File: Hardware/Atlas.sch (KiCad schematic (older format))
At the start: 31 parts, among them U1 MS5611, U2 HTU21D, U3 uSD Card, U4 RFD900, U5 MPU9150, U6 XBEE, U7 VENUS838LPX-L

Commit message: Add 5v regulator and remove before flight switch
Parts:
- added C?: C, ~, symbol C
- added C? (x3): 10uF, CAPC2012-N, symbol C
- added J?: DC, ~, symbol CONN-DC-JACK
- added L?: 4.7uH, INDC-SRN4018, symbol L
- added R?: 52.3k, RESC1608-N, symbol R
- added R?: R, ~, symbol R
- added R?: 10k, RESC1608-N, symbol R
- added U?: AOZ1031, ~, symbol AOZ1031
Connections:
- wire segments 158 -> 193
- no-connect marks 31 -> 40
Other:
- moved on the sheet: B1, H1B, H1C

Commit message: Connect serial peripherals
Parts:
- gave numbers to parts that had none: 10
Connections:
- wire segments 193 -> 267

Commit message: Remove split GPS ground
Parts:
- removed R5: 0, RESC1608-N, symbol R
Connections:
- net labels removed: AGND
- wire segments 267 -> 194

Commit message: Majority of layout and routing
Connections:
- net +5V: no longer H1.D18 (5V)
- net LX: now reaches L2.1, U8.7 (L), U8.8 (L)
- no-connect marks 40 -> 43
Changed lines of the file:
@@
 Sheet 1 1
 Title "Atlas (Nucleo Shield)"
-Date "24 may 2014"
+Date "25 may 2014"
 Rev "1"
 Comp "Aerodyne Labs"
@@
 Connection ~ 2700 9400
 Wire Wire Line
-	2800 8300 2800 9200
-Wire Wire Line
 	2800 8600 2500 8600
-Wire Wire Line
-	2800 9200 2500 9200
-Connection ~ 2800 8600
 Wire Wire Line
 	2600 8300 2600 9100
@@
 	10300 1800 10300 2000
 Connection ~ 10100 2200
+Text Label 14000 1700 2    60   ~ 0
+LX
+Wire Wire Line
+	2800 8300 2800 8600
+NoConn ~ 2500 9200
+NoConn ~ 1500 9000
+NoConn ~ 1500 9100
 $EndSCHEMATC

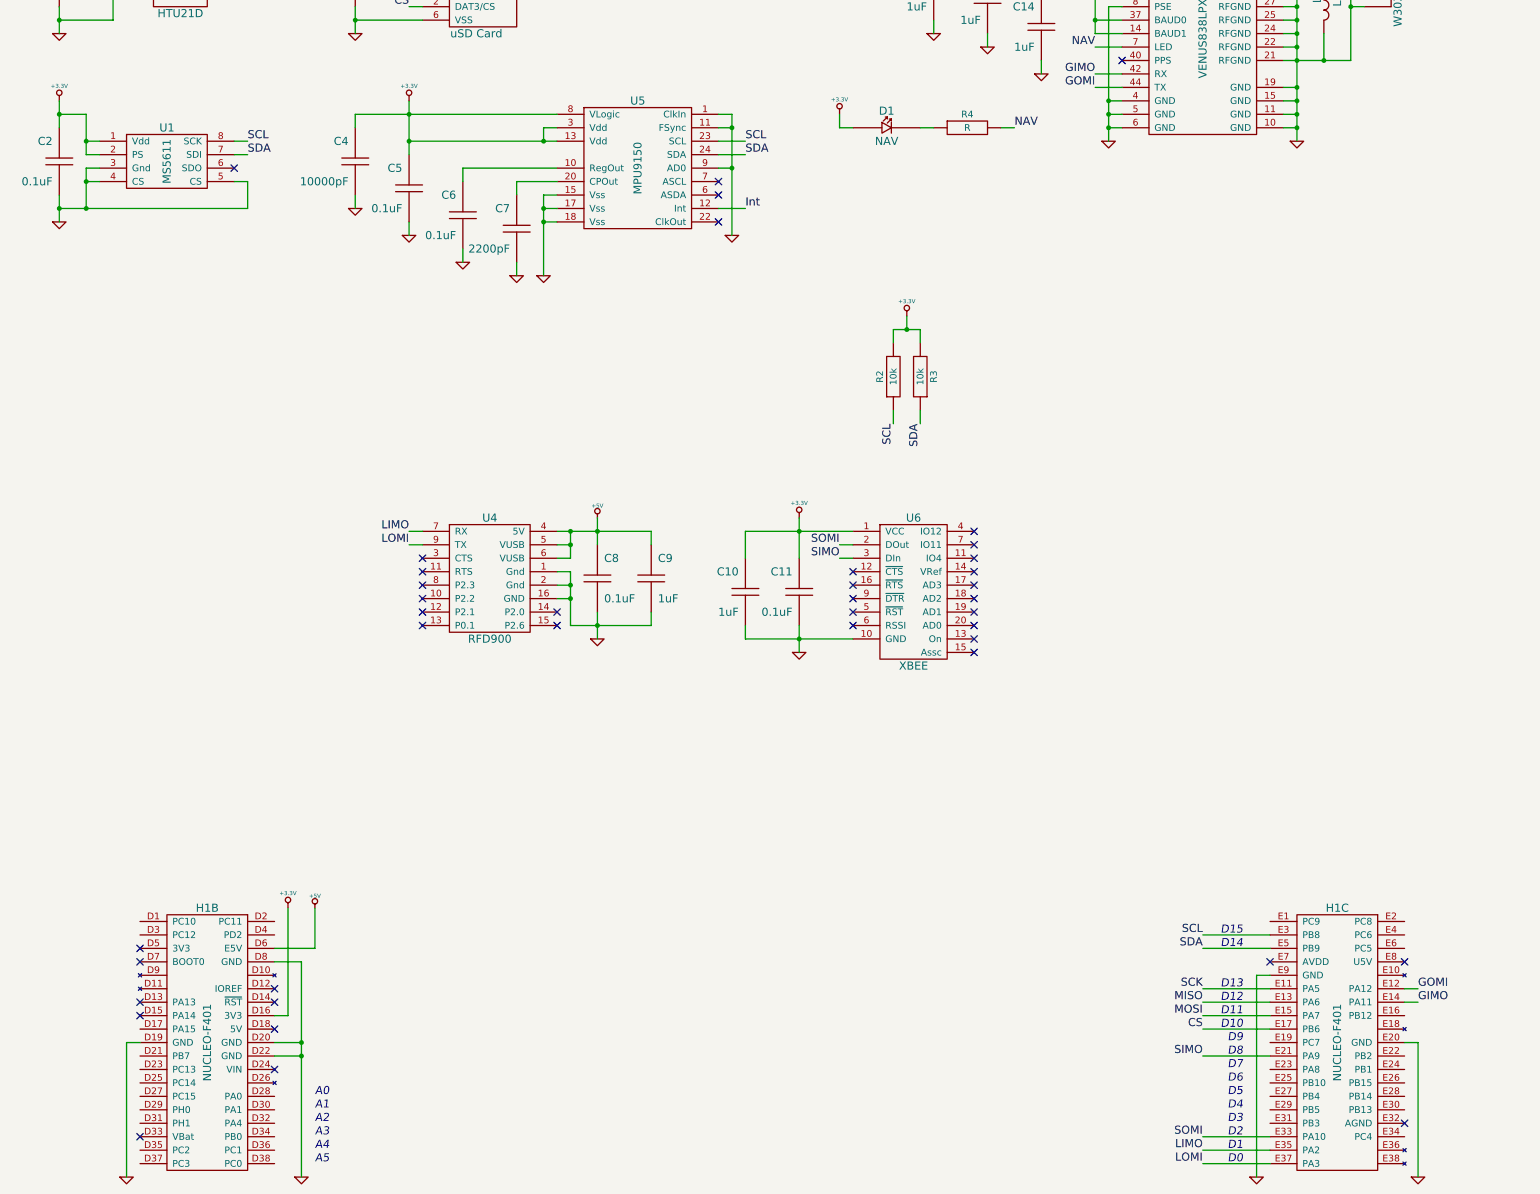
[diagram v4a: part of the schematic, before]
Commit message: Add LEDs
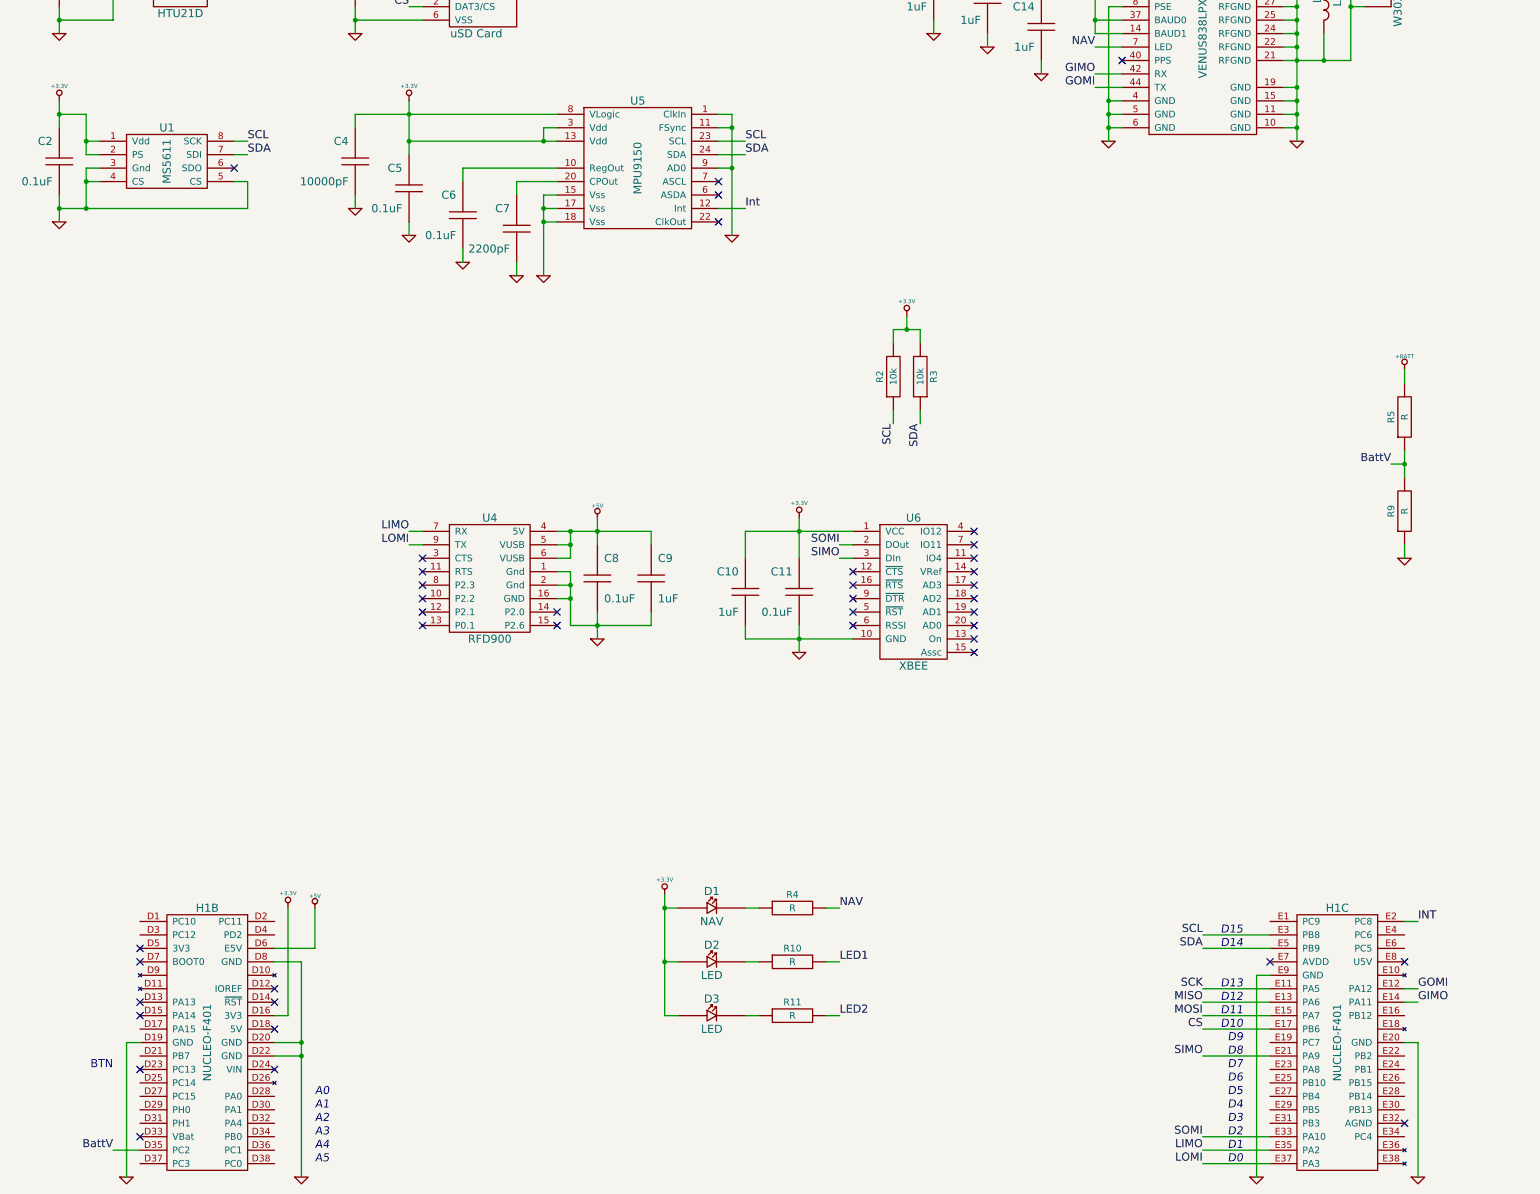
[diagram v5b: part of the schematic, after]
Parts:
- added D2, D3: LED, ~, symbol LED
- added R10, R11, R5, R9: R, ~, symbol R
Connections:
- net +3.3V: now also D2.1, D3.1
- net +BATT: now also R5.2
- net GND: now also R9.1
- net BattV: now reaches H1.D35 (PC2)
- net BattV: now also R5.1, R9.2
- net INT: now reaches H1.E2 (PC8)
- new net: D2.2, R10.1
- new net: D3.2, R11.1
- new net LED1: R10.2
- new net LED2: R11.2
- no-connect marks 43 -> 44
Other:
- note added: "BTN"
- moved on the sheet: D1, R4
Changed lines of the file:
@@
 Sheet 1 1
 Title "Atlas (Nucleo Shield)"
-Date "25 may 2014"
+Date "26 may 2014"
 Rev "1"
 Comp "Aerodyne Labs"
@@
 L LED D1
 U 1 1 537FBE8B
-P 7050 2500
-F 0 "D1" H 7050 2625 60  0000 C CNN
-F 1 "NAV" H 7050 2400 60  0000 C CNN
-F 2 "~" H 7050 2500 60  0000 C CNN
-F 3 "~" H 7050 2500 60  0000 C CNN
-F 4 "V" H 7450 3025 60  0001 C CNN "Voltage"
-F 5 "I" H 7550 3125 60  0001 C CNN "Current"
-	1    7050 2500
-	1    0    0    -1
-$EndComp
-Text Label 8000 2500 0    60   ~ 0
+P 5750 8300
+F 0 "D1" H 5750 8425 60  0000 C CNN
+F 1 "NAV" H 5750 8200 60  0000 C CNN
+F 2 "~" H 5750 8300 60  0000 C CNN
+F 3 "~" H 5750 8300 60  0000 C CNN
+F 4 "V" H 6150 8825 60  0001 C CNN "Voltage"
+F 5 "I" H 6250 8925 60  0001 C CNN "Current"
+	1    5750 8300
+	1    0    0    -1
+$EndComp
+Text Label 6700 8300 0    60   ~ 0
 NAV
 $Comp
 L R R4
 U 1 1 537FBEA6
-P 7650 2500
-F 0 "R4" H 7650 2600 50  0000 C CNN
-F 1 "R" H 7650 2500 50  0000 C CNN
-F 2 "~" H 7650 2500 60  0000 C CNN
-F 3 "~" H 7650 2500 60  0000 C CNN
-F 4 "W" H 7650 2400 50  0001 C CNN "Power"
-F 5 "%" H 7650 2300 50  0001 C CNN "Tolerance"
-	1    7650 2500
+P 6350 8300
+F 0 "R4" H 6350 8400 50  0000 C CNN
+F 1 "R" H 6350 8300 50  0000 C CNN
+F 2 "~" H 6350 8300 60  0000 C CNN
+F 3 "~" H 6350 8300 60  0000 C CNN
+F 4 "W" H 6350 8200 50  0001 C CNN "Power"
+F 5 "%" H 6350 8100 50  0001 C CNN "Tolerance"
+	1    6350 8300
 	1    0    0    -1
 $EndComp
@@
 L +3.3V #PWR023
 U 1 1 537FC261
-P 6700 2400
-F 0 "#PWR023" H 6700 2360 30  0001 C CNN
-F 1 "+3.3V" H 6700 2510 30  0000 C CNN
-F 2 "" H 6700 2400 60  0000 C CNN
-F 3 "" H 6700 2400 60  0000 C CNN
-	1    6700 2400
+P 5400 8200
+F 0 "#PWR023" H 5400 8160 30  0001 C CNN
+F 1 "+3.3V" H 5400 8310 30  0000 C CNN
+F 2 "" H 5400 8200 60  0000 C CNN
+F 3 "" H 5400 8200 60  0000 C CNN
+	1    5400 8200
 	1    0    0    -1
 $EndComp
@@
 	8600 2200 8800 2200
 Wire Wire Line
-	6700 2400 6700 2500
-Wire Wire Line
-	6700 2500 6800 2500
-Wire Wire Line
-	7300 2500 7400 2500
-Wire Wire Line
-	7900 2500 8000 2500
+	5400 8200 5400 9100
+Wire Wire Line
+	5400 8300 5500 8300
+Wire Wire Line
+	6000 8300 6100 8300
+Wire Wire Line
+	6600 8300 6700 8300
 Wire Wire Line
 	10100 1100 10100 2600
@@
 NoConn ~ 1500 9000
 NoConn ~ 1500 9100
+NoConn ~ 1500 9500
+Text Notes 1300 9500 2    60   ~ 0
+BTN
+$Comp
+L R R5
+U 1 1 53829219
+P 10900 4650
+F 0 "R5" H 10900 4750 50  0000 C CNN
+F 1 "R" H 10900 4650 50  0000 C CNN
+F 2 "~" H 10900 4650 60  0000 C CNN
+F 3 "~" H 10900 4650 60  0000 C CNN
+F 4 "W" H 10900 4550 50  0001 C CNN "Power"
+F 5 "%" H 10900 4450 50  0001 C CNN "Tolerance"
+	1    10900 4650
+	0    -1   -1   0
+$EndComp
+$Comp
+L R R9
+U 1 1 53829234
+P 10900 5350
+F 0 "R9" H 10900 5450 50  0000 C CNN
+F 1 "R" H 10900 5350 50  0000 C CNN
+F 2 "~" H 10900 5350 60  0000 C CNN
+F 3 "~" H 10900 5350 60  0000 C CNN
+F 4 "W" H 10900 5250 50  0001 C CNN "Power"
+F 5 "%" H 10900 5150 50  0001 C CNN "Tolerance"
+	1    10900 5350
+	0    -1   -1   0
+$EndComp
+Text Label 10800 5000 2    60   ~ 0
+BattV
+$Comp
+L GND #PWR043
+U 1 1 5382934F
+P 10900 5700
+F 0 "#PWR043" H 10900 5700 30  0001 C CNN
+F 1 "GND" H 10900 5630 30  0001 C CNN
+F 2 "" H 10900 5700 60  0000 C CNN
+F 3 "" H 10900 5700 60  0000 C CNN
+	1    10900 5700
+	1    0    0    -1
+$EndComp
+$Comp
+L +BATT #PWR044
+U 1 1 5382935E
+P 10900 4300
+F 0 "#PWR044" H 10900 4250 20  0001 C CNN
+F 1 "+BATT" H 10900 4400 30  0000 C CNN
+F 2 "" H 10900 4300 60  0000 C CNN
+F 3 "" H 10900 4300 60  0000 C CNN
+	1    10900 4300
+	1    0    0    -1
+$EndComp
+Wire Wire Line
+	10900 4300 10900 4400
+Wire Wire Line
+	10900 4900 10900 5100
+Wire Wire Line
+	10900 5600 10900 5700
+Wire Wire Line
+	10800 5000 10900 5000
+Connection ~ 10900 5000
+Text Label 1300 10100 2    60   ~ 0
+BattV
+Wire Wire Line
+	1300 10100 1500 10100
+Text Label 11000 8400 0    60   ~ 0
+INT
+Wire Wire Line
+	11000 8400 10900 8400
+$Comp
+L LED D2
+U 1 1 5382B2D5
+P 5750 8700
+F 0 "D2" H 5750 8825 60  0000 C CNN
+F 1 "LED" H 5750 8600 60  0000 C CNN
+F 2 "~" H 5750 8700 60  0000 C CNN
+F 3 "~" H 5750 8700 60  0000 C CNN
+F 4 "V" H 6150 9225 60  0001 C CNN "Voltage"
+F 5 "I" H 6250 9325 60  0001 C CNN "Current"
+	1    5750 8700
+	1    0    0    -1
+$EndComp
+$Comp
+L R R10
+U 1 1 5382B2F0
+P 6350 8700
+F 0 "R10" H 6350 8800 50  0000 C CNN
+F 1 "R" H 6350 8700 50  0000 C CNN
+F 2 "~" H 6350 8700 60  0000 C CNN
+F 3 "~" H 6350 8700 60  0000 C CNN
+F 4 "W" H 6350 8600 50  0001 C CNN "Power"
+F 5 "%" H 6350 8500 50  0001 C CNN "Tolerance"
+	1    6350 8700
+	1    0    0    -1
+$EndComp
+$Comp
+L R R11
+U 1 1 5382B30B
+P 6350 9100
+F 0 "R11" H 6350 9200 50  0000 C CNN
+F 1 "R" H 6350 9100 50  0000 C CNN
+F 2 "~" H 6350 9100 60  0000 C CNN
+F 3 "~" H 6350 9100 60  0000 C CNN
+F 4 "W" H 6350 9000 50  0001 C CNN "Power"
+F 5 "%" H 6350 8900 50  0001 C CNN "Tolerance"
+	1    6350 9100
+	1    0    0    -1
+$EndComp
+$Comp
+L LED D3
+U 1 1 5382B326
+P 5750 9100
+F 0 "D3" H 5750 9225 60  0000 C CNN
+F 1 "LED" H 5750 9000 60  0000 C CNN
+F 2 "~" H 5750 9100 60  0000 C CNN
+F 3 "~" H 5750 9100 60  0000 C CNN
+F 4 "V" H 6150 9625 60  0001 C CNN "Voltage"
+F 5 "I" H 6250 9725 60  0001 C CNN "Current"
+	1    5750 9100
+	1    0    0    -1
+$EndComp
+Wire Wire Line
+	5400 8700 5500 8700
+Connection ~ 5400 8300
+Wire Wire Line
+	5400 9100 5500 9100
+Connection ~ 5400 8700
+Wire Wire Line
+	6000 8700 6100 8700
+Wire Wire Line
+	6000 9100 6100 9100
+Text Label 6700 8700 0    60   ~ 0
+LED1
+Text Label 6700 9100 0    60   ~ 0
+LED2
+Wire Wire Line
+	6600 8700 6700 8700
+Wire Wire Line
+	6600 9100 6700 9100
 $EndSCHEMATC

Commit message: Finish PCB
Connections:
- net INT: now also H1.E6 (PC5); no longer H1.E2 (PC8)
- net LED1: now also H1.E2 (PC8)
- net LED2: now also H1.E4 (PC6)
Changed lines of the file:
@@
 Wire Wire Line
 	1300 10100 1500 10100
-Text Label 11000 8400 0    60   ~ 0
+Text Label 11000 8600 0    60   ~ 0
 INT
 Wire Wire Line
@@
 Wire Wire Line
 	6600 9100 6700 9100
+Text Label 11000 8400 0    60   ~ 0
+LED1
+Text Label 11000 8500 0    60   ~ 0
+LED2
+Wire Wire Line
+	10900 8500 11000 8500
+Wire Wire Line
+	10900 8600 11000 8600
 $EndSCHEMATC
